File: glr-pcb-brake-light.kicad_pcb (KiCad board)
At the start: 4 copper layers, 160 x 20 mm, 36 parts

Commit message: überarbeitung pcb, sch mit stecker
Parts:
- removed REF** (x4): MountingHole_3.2mm_M3_Pad, MountingHole:MountingHole_3.2mm_M3_Pad
- removed TP1, TP2: TestPoint, TestPoint:TestPoint_Keystone_5010-5014_Multipurpose
- added J1: Conn_01x04_Pin, GLR_KiCad_Library:Wuerth_M12-Right-Angled-THT, F.Cu at (240.2, 97.9)
- D25, R1, R2, R3, R4: moved to F.Cu
- moved D12 170.5 mm to (32.0, 149.9), turned to 0 degrees
- moved D25 167.3 mm to (26.9, 173.5)
- moved D21 163.8 mm to (38.1, 158.6), turned to 0 degrees
- moved D11 156.4 mm to (32.0, 145.5), turned to 0 degrees
- moved D10 142.3 mm to (32.0, 141.2), turned to 0 degrees
- moved D22 135.2 mm to (44.2, 132.5), turned to 0 degrees
- moved D9 128.3 mm to (32.0, 136.8), turned to 0 degrees
- moved D7 124.3 mm to (25.9, 158.6), turned to 0 degrees
- moved D23 124.3 mm to (44.2, 136.8), turned to 0 degrees
- moved D20 115.1 mm to (38.1, 154.2), turned to 0 degrees
- moved D8 114.4 mm to (32.0, 132.5), turned to 0 degrees
- moved D24 114.2 mm to (44.2, 141.2), turned to 0 degrees
- moved D6 111.7 mm to (25.9, 154.2), turned to 0 degrees
- moved R4 108.6 mm to (53.4, 187.3), turned to 0 degrees
- moved R3 103.7 mm to (53.4, 182.3), turned to 0 degrees
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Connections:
- net Net-(D12-K) renamed GND
- D25 pad 2: Net-(D25-A) -> +24V
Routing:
- net GND: track 149.3 -> 0.00 mm
- net Net-(D25-K): track 132.0 -> 0.00 mm
- net Net-(D7-A): track 74.3 -> 0.00 mm, vias 1 -> 0
- net Net-(D19-A): track 68.4 -> 0.00 mm, vias 1 -> 0
- net Net-(D20-K): track 56.7 -> 0.00 mm
- net Net-(D13-A): track 22.0 -> 0.00 mm, vias 1 -> 0
- net Net-(D3-K): track 17.1 -> 0.00 mm
- net Net-(D16-K): track 15.9 -> 0.00 mm
- net Net-(D5-K): track 15.9 -> 0.00 mm
- net Net-(D8-K): track 15.9 -> 0.00 mm
- net Net-(D4-K): track 15.4 -> 0.00 mm
- net Net-(D23-K): track 15.4 -> 0.00 mm
- net Net-(D22-K): track 15.4 -> 0.00 mm
- net Net-(D10-A): track 15.4 -> 0.00 mm
- net Net-(D13-K): track 15.4 -> 0.00 mm
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- added copper zone on B.Cu, net GND
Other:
- board size 160 x 20 mm -> 190 x 26 mm
- copper layers 4 -> 2

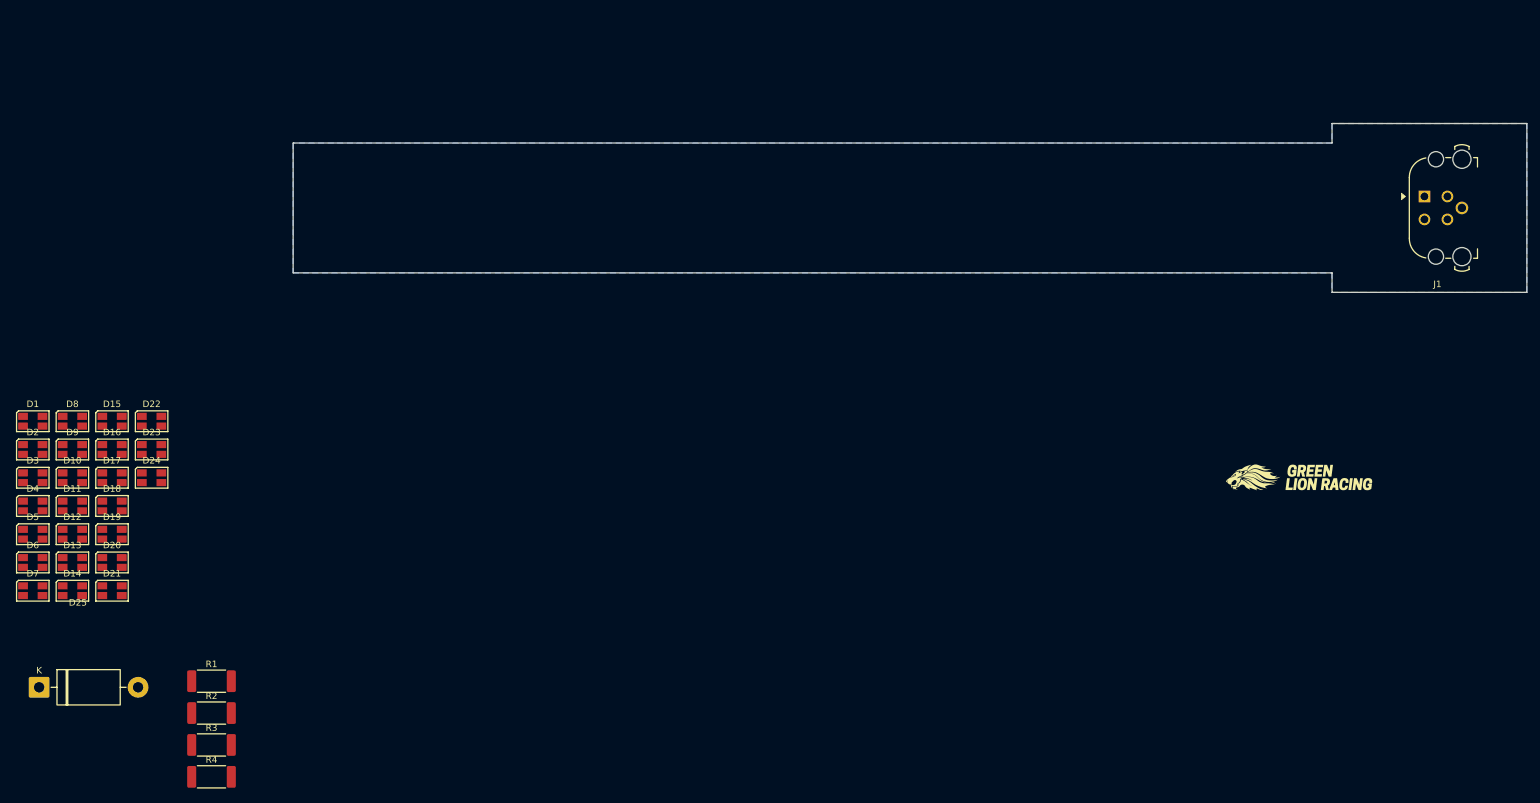
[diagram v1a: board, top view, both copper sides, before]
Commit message: PCB anordnung
pcb fast fertig routing fehlt und 3D modelle teilweise
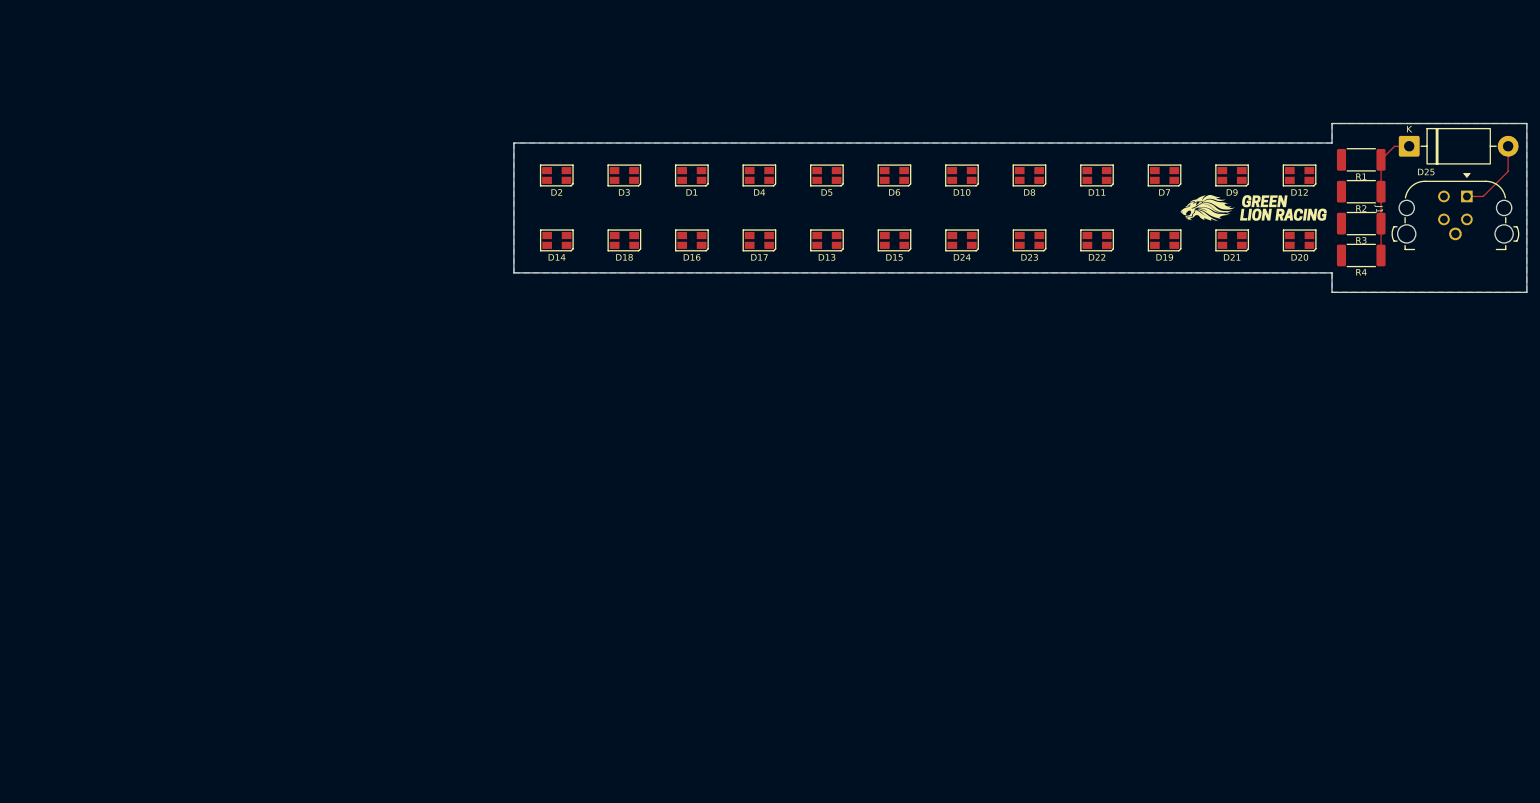
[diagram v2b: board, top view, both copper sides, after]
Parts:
- moved D25 226.9 mm to (237.9, 90.1)
- moved D12 196.9 mm to (221.0, 94.6), turned to 180 degrees
- moved R1 194.4 mm to (230.5, 92.2), turned to 180 degrees
- moved R2 194.4 mm to (230.5, 97.1), turned to 180 degrees
- moved R3 194.4 mm to (230.5, 102.0), turned to 180 degrees
- moved R4 194.4 mm to (230.5, 107.0), turned to 180 degrees
- moved D20 189.5 mm to (221.0, 104.6), turned to 180 degrees
- moved D7 185.7 mm to (200.2, 94.6), turned to 180 degrees
- moved D9 183.5 mm to (210.6, 94.6), turned to 180 degrees
- moved D21 180.8 mm to (210.6, 104.6), turned to 180 degrees
- moved D19 168.3 mm to (200.2, 104.6), turned to 180 degrees
- moved D11 165.8 mm to (189.8, 94.6), turned to 180 degrees
- moved D8 152.2 mm to (179.4, 94.6), turned to 180 degrees
- moved D22 148.3 mm to (189.8, 104.6), turned to 180 degrees
- moved D6 145.5 mm to (158.6, 94.6), turned to 180 degrees
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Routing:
- net Net-(D25-K): track 0.00 -> 19.9 mm
- net +24V: track 0.00 -> 11.8 mm
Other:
- board size 190 x 26 mm -> 156 x 26 mm

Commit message: pcb fertig
änderungen vielleicht noch an der diode vornehmen eventuell kleiner dimensionieren
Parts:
- moved D24 52.0 mm to (221.0, 104.6)
- moved D20 41.6 mm to (179.4, 104.6)
- moved D13 41.6 mm to (106.6, 104.6)
- moved D18 41.6 mm to (158.6, 104.6)
- moved D19 31.2 mm to (169.0, 104.6)
- moved D15 31.2 mm to (127.4, 104.6)
- moved D10 31.2 mm to (200.2, 94.6)
- moved D7 31.2 mm to (169.0, 94.6)
- moved D23 31.2 mm to (210.6, 104.6)
- moved D21 20.8 mm to (189.8, 104.6)
- moved D11 20.8 mm to (210.6, 94.6)
- moved D9 20.8 mm to (189.8, 94.6)
- moved D1 20.8 mm to (106.6, 94.6)
- moved D2 10.4 mm to (117.0, 94.6)
- moved D3 10.4 mm to (127.4, 94.6)
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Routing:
- net Net-(D1-A): track 0.00 -> 128.3 mm
- net Net-(D13-A): track 0.00 -> 124.8 mm
- net Net-(D19-A): track 0.00 -> 66.4 mm
- net Net-(D7-A): track 0.00 -> 62.2 mm
- net GND: track 0.00 -> 9.00 mm, vias 0 -> 4
- net Net-(D8-K): track 0.00 -> 7.40 mm
- net Net-(D7-K): track 0.00 -> 7.40 mm
- net Net-(D5-K): track 0.00 -> 7.40 mm
- net Net-(D4-K): track 0.00 -> 7.40 mm
- net Net-(D3-K): track 0.00 -> 7.40 mm
- net Net-(D22-K): track 0.00 -> 7.40 mm
- net Net-(D21-K): track 0.00 -> 7.40 mm
- net Net-(D20-K): track 0.00 -> 7.40 mm
- net Net-(D19-K): track 0.00 -> 7.40 mm
- net Net-(D17-K): track 0.00 -> 7.40 mm
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
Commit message: pcb umdesigned fast fertig
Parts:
- J1: footprint GLR_KiCad_Library:Wuerth_M12-Right-Angled-THT -> GLR_KiCad_Library:Wuerth_M12-Panel-Cut-THT; moved to B.Cu
- moved R3 104.8 mm to (126.1, 98.3)
- moved R1 104.5 mm to (126.1, 89.6)
- moved D25 101.3 mm to (136.7, 92.8)
- moved J1 85.7 mm to (161.3, 93.0), turned to 180 degrees
- moved R2 51.3 mm to (179.6, 90.6), turned to 0 degrees
- moved R4 51.1 mm to (179.6, 97.7), turned to 0 degrees
- moved D1 11.1 mm to (106.6, 83.5)
- moved D10 11.1 mm to (200.2, 83.5)
- moved D11 11.1 mm to (210.6, 83.5)
- moved D12 11.1 mm to (221.0, 83.5)
- moved D2 11.1 mm to (117.0, 83.5)
- moved D3 11.1 mm to (127.4, 83.5)
- moved D4 11.1 mm to (137.8, 83.5)
- moved D5 11.1 mm to (148.2, 83.5)
- moved D6 11.1 mm to (158.6, 83.5)
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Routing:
- net Net-(D13-A): track 124.8 -> 0.00 mm
- net Net-(D1-A): track 128.3 -> 21.6 mm
- net Net-(D7-A): track 62.2 -> 18.5 mm
- net Net-(D19-A): track 66.4 -> 25.0 mm
- net Net-(D25-K): track 19.9 -> 32.4 mm
- net +24V: track 11.8 -> 9.40 mm
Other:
- board size 156 x 26 mm -> 126 x 30 mm

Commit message: mounting holes
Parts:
- added REF**: MountingHole_2.2mm_M2_ISO7380, MountingHole:MountingHole_2.2mm_M2_ISO7380, F.Cu at (153.1, 94.2)
- added REF**: MountingHole_2.2mm_M2_ISO7380, MountingHole:MountingHole_2.2mm_M2_ISO7380, F.Cu at (173.5, 94.4)
- moved D25 2.96 mm to (133.7, 92.6)
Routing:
- net Net-(D25-K): track 32.4 -> 70.6 mm
- net Net-(D13-A): track 0.00 -> 26.4 mm
- net +24V: track 9.40 -> 13.6 mm

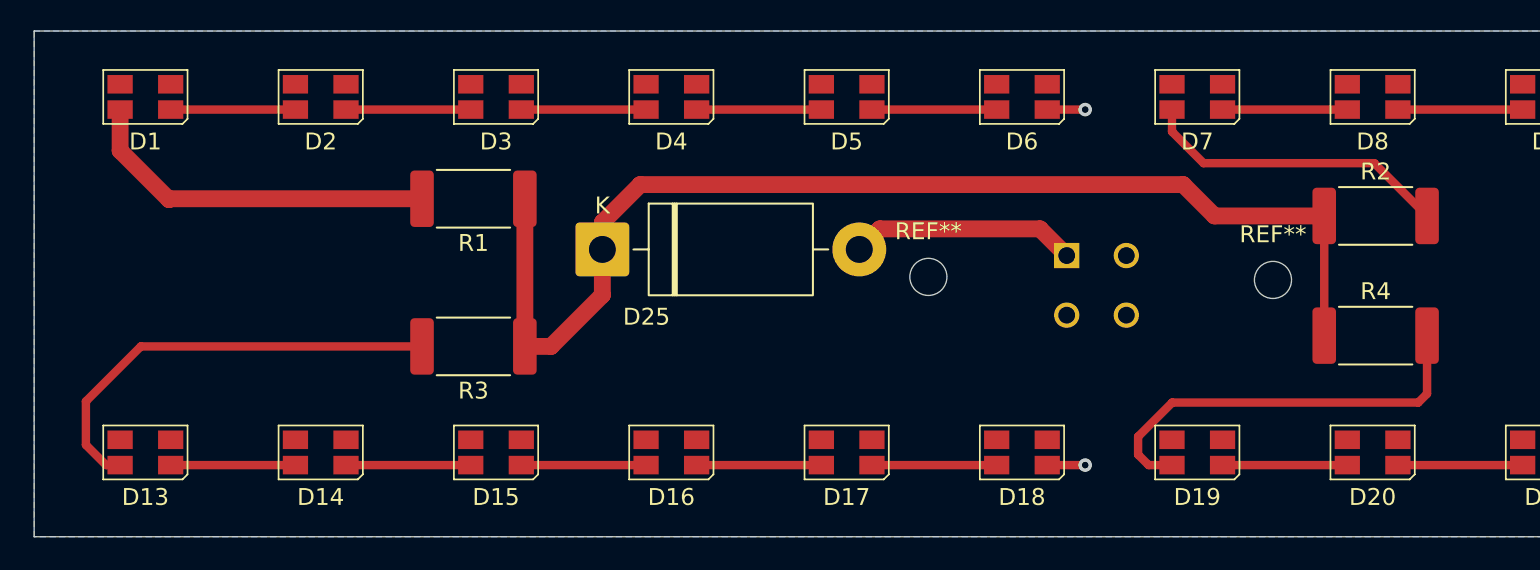
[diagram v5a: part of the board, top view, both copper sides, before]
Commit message: teile auf rückseite gebracht
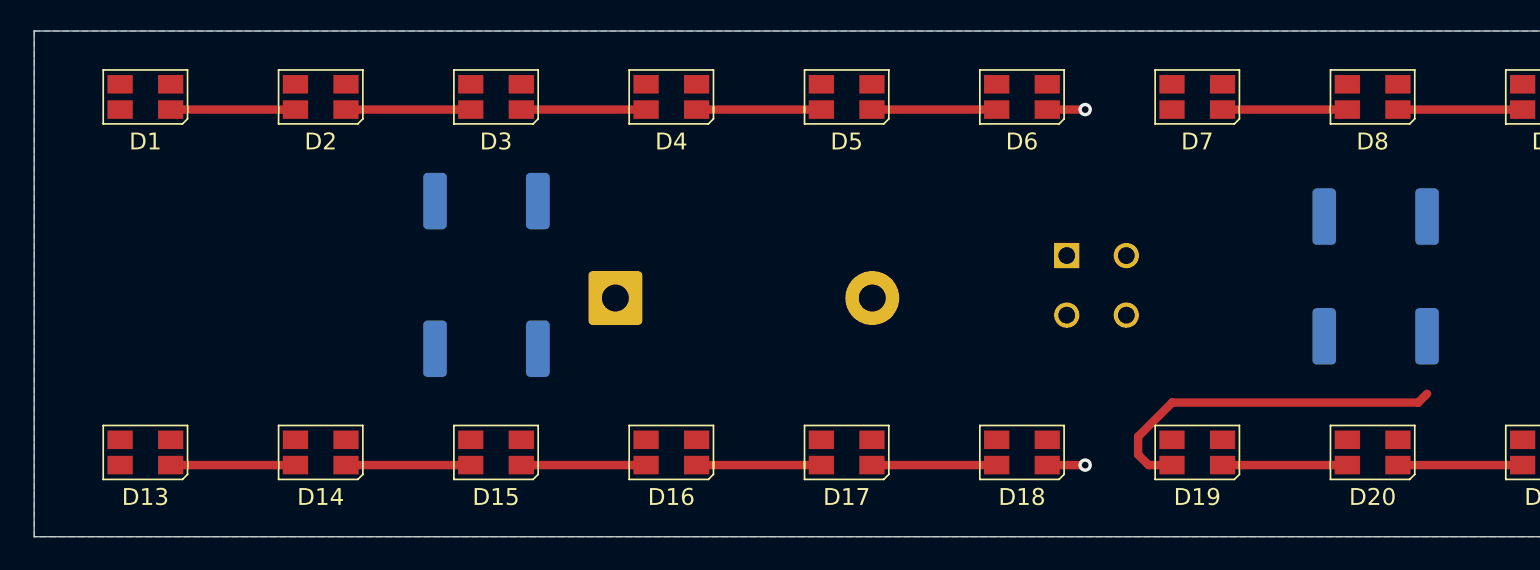
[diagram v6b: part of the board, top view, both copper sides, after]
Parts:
- removed REF** (x2): MountingHole_2.2mm_M2_ISO7380, MountingHole:MountingHole_2.2mm_M2_ISO7380
- D1, D10, D11, D12, D13, D14, D15, D16, D17, D18, D19, D2, D20, D21, D22, D23, D24, D3, D4, D5, D6, D7, D8, D9: footprint LED_SMD:LED_Avago_PLCC4_3.2x2.8mm_CW -> GLR_KiCad_Library:LED_Avago_PLCC4_3.2x2.8mm_CW
- D25, R1, R2, R3, R4: moved to B.Cu
- moved R1 8.93 mm to (126.8, 98.5)
- moved R3 8.66 mm to (126.8, 89.7)
- moved R2 7.14 mm to (179.6, 97.8)
- moved R4 7.06 mm to (179.6, 90.7)
- moved D25 2.98 mm to (134.5, 95.5)
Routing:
- net Net-(D25-K): track 70.6 -> 0.00 mm
- net Net-(D13-A): track 26.4 -> 0.00 mm
- net Net-(D1-A): track 21.6 -> 0.00 mm
- net Net-(D7-A): track 18.5 -> 0.00 mm
- net +24V: track 13.6 -> 0.00 mm
- net Net-(D19-A): track 25.0 -> 21.5 mm
